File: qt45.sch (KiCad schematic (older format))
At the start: 106 parts, among them SW1 SW_PUSH, U1 ATmega32U4-AU, Y1 16MHz

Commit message: Layout key switches
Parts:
- removed MX42: MX-1U, MX_Alps_Hybrid:MXOnly-1U-NoLED, symbol MX_Alps_Hybrids:MX-1U
- added MX42: MX-1.25U, MX_Alps_Hybrid:MXOnly-1.25U-NoLED, symbol MX_Alps_Hybrids:MX-1.25U
- renumbered D5 to D3, D3 to D4, D4 to D5
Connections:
- net COL12: now also MX42.1 (COL)
- net at D42.2 (A): now also MX42.2 (ROW)
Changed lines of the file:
@@
 $EndComp
 $Comp
-L Device:D_Small D3
+L Device:D_Small D4
 U 1 1 5C9F1A36
 P 6500 3725
-F 0 "D3" H 6500 3875 50  0000 R CNN
+F 0 "D4" H 6500 3875 50  0000 R CNN
 F 1 "SOD-123" H 6900 3875 50  0000 R CNN
 F 2 "random-keyboard-parts:D_SOD-123-Pretty" V 6500 3725 50  0001 C CNN
@@
 $EndComp
 $Comp
-L Device:D_Small D4
+L Device:D_Small D5
 U 1 1 5C9F3E7F
 P 6500 4475
-F 0 "D4" H 6500 4625 50  0000 R CNN
+F 0 "D5" H 6500 4625 50  0000 R CNN
 F 1 "SOD-123" H 6900 4625 50  0000 R CNN
 F 2 "random-keyboard-parts:D_SOD-123-Pretty" V 6500 4475 50  0001 C CNN
@@
 COL13
 $Comp
-L Device:D_Small D5
+L Device:D_Small D3
 U 1 1 5C9E3060
 P 5750 5225
-F 0 "D5" H 5750 5375 50  0000 R CNN
+F 0 "D3" H 5750 5375 50  0000 R CNN
 F 1 "SOD-123" H 6150 5375 50  0000 R CNN
 F 2 "random-keyboard-parts:D_SOD-123-Pretty" V 5750 5225 50  0001 C CNN
@@
 Wire Wire Line
 	14300 4925 14300 4175
-$Comp
-L MX_Alps_Hybrids:MX-1U MX42
-U 1 1 5CA77763
-P 14875 4950
-F 0 "MX42" H 14961 5167 60  0000 C CNN
-F 1 "MX-1U" H 14961 5093 20  0000 C CNN
-F 2 "MX_Alps_Hybrid:MXOnly-1U-NoLED" H 14850 4925 60  0001 C CNN
-F 3 "" H 14850 4925 60  0001 C CNN
-	1    14875 4950
-	1    0    0    -1
-$EndComp
 $Comp
 L Device:D_Small D42
@@
 	14300 5675 14300 4925
 Connection ~ 14300 4925
+$Comp
+L MX_Alps_Hybrids:MX-1.25U MX42
+U 1 1 5CB0FADC
+P 14875 4950
+F 0 "MX42" H 14961 5167 60  0000 C CNN
+F 1 "MX-1.25U" H 14961 5093 20  0000 C CNN
+F 2 "MX_Alps_Hybrid:MXOnly-1.25U-NoLED" H 14850 4925 60  0001 C CNN
+F 3 "" H 14850 4925 60  0001 C CNN
+	1    14875 4950
+	1    0    0    -1
+$EndComp
 $EndSCHEMATC

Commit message: Rough placement of components
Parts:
- MX23: footprint MX_Alps_Hybrid:MXOnly-6.25U-NoLED -> MX_Alps_Hybrid:MXOnly-6.25U-ReversedStabilizers-NoLED
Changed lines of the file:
@@
 F 0 "MX23" H 10461 5917 60  0000 C CNN
 F 1 "MX-6.25U" H 10461 5843 20  0000 C CNN
-F 2 "MX_Alps_Hybrid:MXOnly-6.25U-NoLED" H 10350 5675 60  0001 C CNN
+F 2 "MX_Alps_Hybrid:MXOnly-6.25U-ReversedStabilizers-NoLED" H 10350 5675 60  0001 C CNN
 F 3 "" H 10350 5675 60  0001 C CNN
 	1    10375 5700

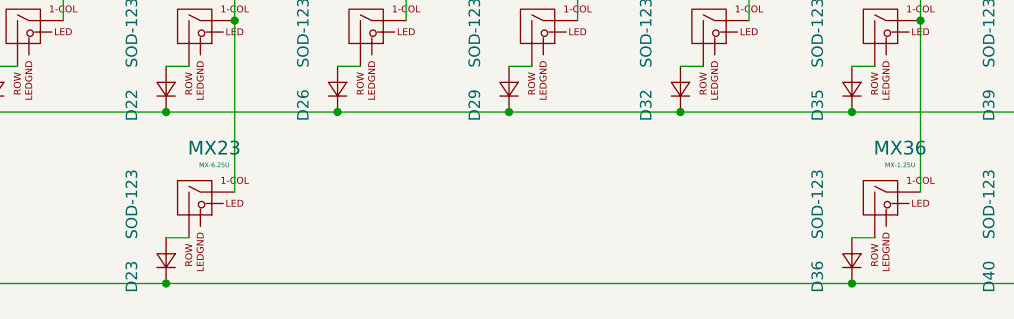
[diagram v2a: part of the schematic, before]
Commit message: Routing (no rows and columns)
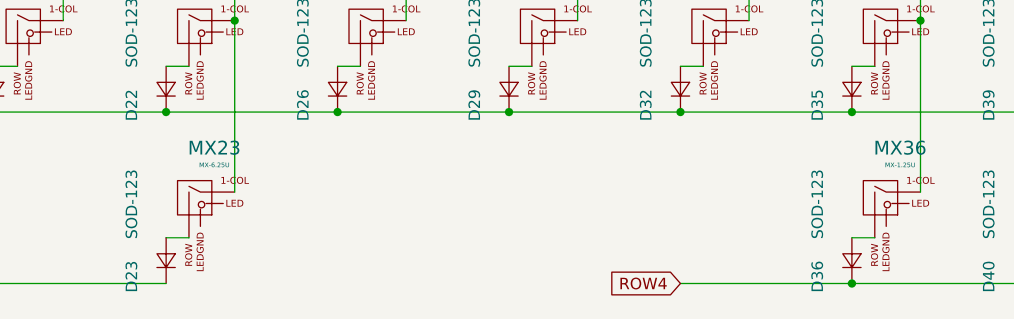
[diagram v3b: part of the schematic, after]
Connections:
- net ROW3: no longer D36.1 (K), D40.1 (K)
- new net ROW4: D36.1 (K), D40.1 (K)
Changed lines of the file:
@@
 	13250 5875 13350 5875
-Wire Wire Line
-	13250 6075 10250 6075
 Wire Wire Line
 	13550 5675 13550 4925
@@
 Wire Wire Line
 	14000 6075 13250 6075
-Connection ~ 10250 6075
-Connection ~ 13250 6075
 $Comp
 L MX_Alps_Hybrids:MX-1.25U MX36
@@
 	1    0    0    -1
 $EndComp
+Text GLabel 12500 6075 0    50   Input ~ 0
+ROW4
+Wire Wire Line
+	13250 6075 12500 6075
+Connection ~ 13250 6075
 $EndSCHEMATC

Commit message: Start reroute
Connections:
- net COL6: no longer MX23.1 (COL)
- net COL7: now also MX23.1 (COL)
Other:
- moved on the sheet: D23, MX23
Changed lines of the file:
@@
 L Device:D_Small D23
 U 1 1 5CA86F72
-P 10250 5975
-F 0 "D23" H 10250 6125 50  0000 R CNN
-F 1 "SOD-123" H 10650 6125 50  0000 R CNN
-F 2 "random-keyboard-parts:D_SOD-123-Pretty" V 10250 5975 50  0001 C CNN
-F 3 "~" V 10250 5975 50  0001 C CNN
-	1    10250 5975
+P 11000 5975
+F 0 "D23" H 11000 6125 50  0000 R CNN
+F 1 "SOD-123" H 11400 6125 50  0000 R CNN
+F 2 "random-keyboard-parts:D_SOD-123-Pretty" V 11000 5975 50  0001 C CNN
+F 3 "~" V 11000 5975 50  0001 C CNN
+	1    11000 5975
 	0    -1   -1   0
 $EndComp
 Wire Wire Line
-	10250 5875 10350 5875
+	11000 5875 11100 5875
 Wire Wire Line
-	10250 6075 8000 6075
+	11000 6075 8000 6075
 Wire Wire Line
-	10550 5675 10550 4925
+	11300 5675 11300 4925
 $Comp
 L MX_Alps_Hybrids:MX-6.25U MX23
 U 1 1 5CA8EADA
-P 10375 5700
-F 0 "MX23" H 10461 5917 60  0000 C CNN
-F 1 "MX-6.25U" H 10461 5843 20  0000 C CNN
-F 2 "MX_Alps_Hybrid:MXOnly-6.25U-ReversedStabilizers-NoLED" H 10350 5675 60  0001 C CNN
-F 3 "" H 10350 5675 60  0001 C CNN
-	1    10375 5700
+P 11125 5700
+F 0 "MX23" H 11211 5917 60  0000 C CNN
+F 1 "MX-6.25U" H 11211 5843 20  0000 C CNN
+F 2 "MX_Alps_Hybrid:MXOnly-6.25U-ReversedStabilizers-NoLED" H 11100 5675 60  0001 C CNN
+F 3 "" H 11100 5675 60  0001 C CNN
+	1    11125 5700
 	1    0    0    -1
 $EndComp
-Connection ~ 8000 6075
 $Comp
 L Device:D_Small D36
@@
 Connection ~ 9500 5325
 Connection ~ 10250 5325
-Connection ~ 10550 4925
 Connection ~ 11000 5325
 Connection ~ 11750 5325
@@
 	13250 6075 12500 6075
 Connection ~ 13250 6075
+Connection ~ 11300 4925
+Connection ~ 8000 6075
 $EndSCHEMATC

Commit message: More routing
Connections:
- net COL0: now also U1.31 (PC6)
- net COL1: now also U1.32 (PC7)
- net COL2: now also U1.30 (PB6)
- net COL3: now also U1.29 (PB5)
- net COL4: now also U1.28 (PB4)
- net COL5: now also U1.22 (PD5)
- net COL6: now also U1.27 (PD7)
- net ROW0: now also U1.19 (PD1)
- net ROW1: now also U1.20 (PD2)
- net ROW2: now also U1.21 (PD3)
- net ROW3: now also U1.18 (PD0); no longer D23.1 (K)
- net ROW4: now also D23.1 (K)
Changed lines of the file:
@@
 	11000 5875 11100 5875
-Wire Wire Line
-	11000 6075 8000 6075
 Wire Wire Line
 	11300 5675 11300 4925
@@
 	1    0    0    -1
 $EndComp
-Text GLabel 12500 6075 0    50   Input ~ 0
+Text GLabel 10250 6075 0    50   Input ~ 0
 ROW4
 Wire Wire Line
-	13250 6075 12500 6075
+	13250 6075 11000 6075
 Connection ~ 13250 6075
 Connection ~ 11300 4925
-Connection ~ 8000 6075
+Connection ~ 11000 6075
+Wire Wire Line
+	11000 6075 10250 6075
+Text GLabel 3350 3850 2    50   Input ~ 0
+COL6
+Text GLabel 3350 3650 2    50   Input ~ 0
+COL5
+Text GLabel 3350 2350 2    50   Input ~ 0
+COL4
+Text GLabel 3350 2450 2    50   Input ~ 0
+COL3
+Text GLabel 3350 2550 2    50   Input ~ 0
+COL2
+Text GLabel 3350 2950 2    50   Input ~ 0
+COL1
+Text GLabel 3350 2850 2    50   Input ~ 0
+COL0
+Text GLabel 3350 3450 2    50   Input ~ 0
+ROW2
+Text GLabel 3350 3350 2    50   Input ~ 0
+ROW1
+Text GLabel 3350 3150 2    50   Input ~ 0
+ROW3
+Text GLabel 3350 3250 2    50   Input ~ 0
+ROW0
 $EndSCHEMATC

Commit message: First draft of routing
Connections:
- net ROW4 is gone; now on net ROW3: D23.1 (K), D36.1 (K), D40.1 (K)
- net COL0: now also U1.29 (PB5); no longer U1.31 (PC6)
- net COL1: now also U1.30 (PB6); no longer U1.32 (PC7)
- net COL10: now also U1.38 (PF5)
- net COL11: now also U1.1 (PE6)
- net COL12: now also U1.39 (PF4)
- net COL13: now also U1.40 (PF1)
- net COL2: now also U1.28 (PB4); no longer U1.30 (PB6)
- net COL3: now also U1.27 (PD7); no longer U1.29 (PB5)
- net COL4: now also U1.26 (PD6); no longer U1.28 (PB4)
- net COL6: now also U1.25 (PD4); no longer U1.27 (PD7)
- net COL7: now also U1.41 (PF0)
- net COL8: now also U1.36 (PF7)
- net COL9: now also U1.37 (PF6)
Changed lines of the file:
@@
 	1    0    0    -1
 $EndComp
-Text GLabel 10250 6075 0    50   Input ~ 0
-ROW4
 Wire Wire Line
 	13250 6075 11000 6075
@@
 Connection ~ 11000 6075
 Wire Wire Line
-	11000 6075 10250 6075
-Text GLabel 3350 3850 2    50   Input ~ 0
+	11000 6075 8000 6075
+Text GLabel 3350 3550 2    50   Input ~ 0
 COL6
 Text GLabel 3350 3650 2    50   Input ~ 0
 COL5
-Text GLabel 3350 2350 2    50   Input ~ 0
+Text GLabel 3350 3750 2    50   Input ~ 0
 COL4
-Text GLabel 3350 2450 2    50   Input ~ 0
+Text GLabel 3350 3850 2    50   Input ~ 0
 COL3
 Text GLabel 3350 2550 2    50   Input ~ 0
-COL2
-Text GLabel 3350 2950 2    50   Input ~ 0
 COL1
-Text GLabel 3350 2850 2    50   Input ~ 0
+Text GLabel 3350 2450 2    50   Input ~ 0
 COL0
 Text GLabel 3350 3450 2    50   Input ~ 0
@@
 Text GLabel 3350 3250 2    50   Input ~ 0
 ROW0
+Connection ~ 8000 6075
+Text GLabel 3350 4150 2    50   Input ~ 0
+COL11
+Text GLabel 3350 2350 2    50   Input ~ 0
+COL2
+Text GLabel 3350 4350 2    50   Input ~ 0
+COL7
+Text GLabel 3350 4450 2    50   Input ~ 0
+COL13
+Text GLabel 3350 4550 2    50   Input ~ 0
+COL12
+Text GLabel 3350 4650 2    50   Input ~ 0
+COL10
+Text GLabel 3350 4750 2    50   Input ~ 0
+COL9
+Text GLabel 3350 4850 2    50   Input ~ 0
+COL8
 $EndSCHEMATC

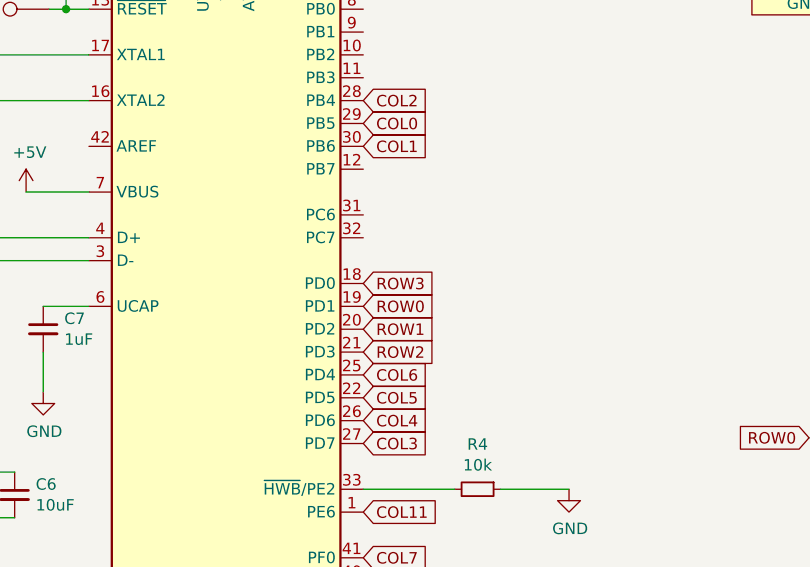
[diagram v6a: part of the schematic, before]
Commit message: Re-route to maximise ground plane
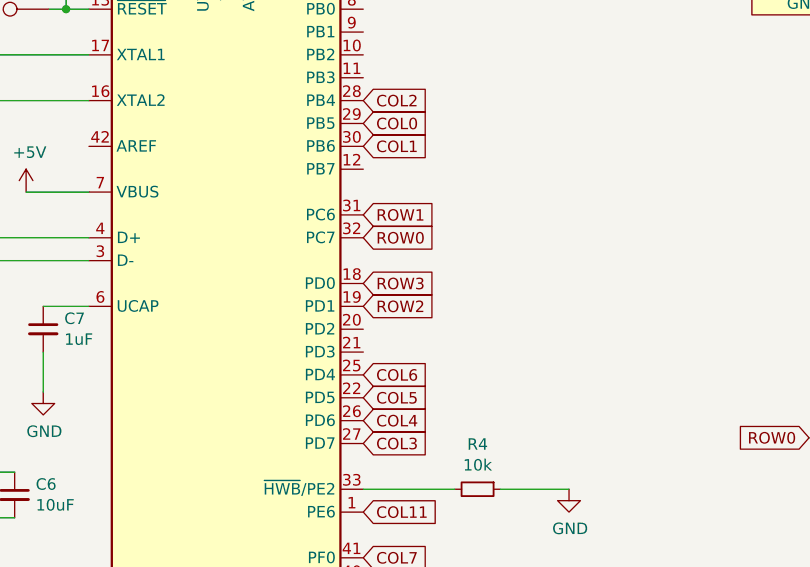
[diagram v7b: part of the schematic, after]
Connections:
- net ROW0: now also U1.32 (PC7); no longer U1.19 (PD1)
- net ROW1: now also U1.31 (PC6); no longer U1.20 (PD2)
- net ROW2: now also U1.19 (PD1); no longer U1.21 (PD3)
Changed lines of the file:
@@
 EESchema Schematic File Version 4
+LIBS:qt45-cache
 EELAYER 29 0
 EELAYER END
@@
 Text GLabel 3350 2450 2    50   Input ~ 0
 COL0
-Text GLabel 3350 3450 2    50   Input ~ 0
+Text GLabel 3350 3250 2    50   Input ~ 0
 ROW2
-Text GLabel 3350 3350 2    50   Input ~ 0
+Text GLabel 3350 2850 2    50   Input ~ 0
 ROW1
 Text GLabel 3350 3150 2    50   Input ~ 0
 ROW3
-Text GLabel 3350 3250 2    50   Input ~ 0
+Text GLabel 3350 2950 2    50   Input ~ 0
 ROW0
 Connection ~ 8000 6075

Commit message: Fix some issues
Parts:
- MX1, MX10, MX11, MX12, MX14, MX15, MX16, MX17, MX18, MX19, MX20, MX21, MX22, MX24, MX25, MX26, MX27, MX28, MX29, MX30, MX31, MX32, MX33, MX34, MX35, MX37, MX38, MX39, MX4, MX40, MX41, MX43, MX45, MX5, MX6, MX7, MX8, MX9: symbol MX_Alps_Hybrids:MX-1U -> qt45-rescue:MX-1U-MX_Alps_Hybrids
- MX13, MX2, MX36, MX42: symbol MX_Alps_Hybrids:MX-1.25U -> qt45-rescue:MX-1.25U-MX_Alps_Hybrids
- MX23: symbol MX_Alps_Hybrids:MX-6.25U -> qt45-rescue:MX-6.25U-MX_Alps_Hybrids
- MX3, MX44: symbol MX_Alps_Hybrids:MX-1.75U -> qt45-rescue:MX-1.75U-MX_Alps_Hybrids
- USB1: symbol random-keyboard-parts:Molex-0548190589 -> qt45-rescue:Molex-0548190589-random-keyboard-parts
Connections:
- net ROW2: now also U1.21 (PD3); no longer U1.19 (PD1)
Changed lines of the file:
@@
 D-
 $Comp
-L random-keyboard-parts:Molex-0548190589 USB1
+L qt45-rescue:Molex-0548190589-random-keyboard-parts USB1
 U 1 1 5C9D7E35
 P 5300 1725
@@
 	6300 1525 6600 1525
 $Comp
-L MX_Alps_Hybrids:MX-1U MX1
+L qt45-rescue:MX-1U-MX_Alps_Hybrids MX1
 U 1 1 5C9E3362
 P 5875 3450
@@
 	5750 3625 5850 3625
 $Comp
-L MX_Alps_Hybrids:MX-1U MX4
+L qt45-rescue:MX-1U-MX_Alps_Hybrids MX4
 U 1 1 5C9F1A30
 P 6625 3450
@@
 	5750 4375 5850 4375
 $Comp
-L MX_Alps_Hybrids:MX-1U MX5
+L qt45-rescue:MX-1U-MX_Alps_Hybrids MX5
 U 1 1 5C9F3E79
 P 6625 4200
@@
 	5600 1925 5750 1925
 $Comp
-L MX_Alps_Hybrids:MX-1.25U MX2
+L qt45-rescue:MX-1.25U-MX_Alps_Hybrids MX2
 U 1 1 5C9B916B
 P 5875 4200
@@
 $EndComp
 $Comp
-L MX_Alps_Hybrids:MX-1U MX6
+L qt45-rescue:MX-1U-MX_Alps_Hybrids MX6
 U 1 1 5C9BC6F1
 P 7375 3450
@@
 	7550 3425 7550 2925
 $Comp
-L MX_Alps_Hybrids:MX-1U MX10
+L qt45-rescue:MX-1U-MX_Alps_Hybrids MX10
 U 1 1 5C9BE4D7
 P 8125 3450
@@
 	8300 3425 8300 2925
 $Comp
-L MX_Alps_Hybrids:MX-1U MX14
+L qt45-rescue:MX-1U-MX_Alps_Hybrids MX14
 U 1 1 5C9C001E
 P 8875 3450
@@
 	9050 3425 9050 2925
 $Comp
-L MX_Alps_Hybrids:MX-1U MX17
+L qt45-rescue:MX-1U-MX_Alps_Hybrids MX17
 U 1 1 5C9C1BBC
 P 9625 3450
@@
 	9800 3425 9800 2925
 $Comp
-L MX_Alps_Hybrids:MX-1U MX20
+L qt45-rescue:MX-1U-MX_Alps_Hybrids MX20
 U 1 1 5C9C3BA7
 P 10375 3450
@@
 	10550 3425 10550 2925
 $Comp
-L MX_Alps_Hybrids:MX-1U MX24
+L qt45-rescue:MX-1U-MX_Alps_Hybrids MX24
 U 1 1 5C9C5CC1
 P 11125 3450
@@
 	11300 3425 11300 2925
 $Comp
-L MX_Alps_Hybrids:MX-1U MX27
+L qt45-rescue:MX-1U-MX_Alps_Hybrids MX27
 U 1 1 5C9C7E50
 P 11875 3450
@@
 	12050 3425 12050 2925
 $Comp
-L MX_Alps_Hybrids:MX-1U MX30
+L qt45-rescue:MX-1U-MX_Alps_Hybrids MX30
 U 1 1 5C9CA35D
 P 12625 3450
@@
 	12800 3425 12800 2925
 $Comp
-L MX_Alps_Hybrids:MX-1U MX33
+L qt45-rescue:MX-1U-MX_Alps_Hybrids MX33
 U 1 1 5C9CC78F
 P 13375 3450
@@
 	13250 3825 12500 3825
 $Comp
-L MX_Alps_Hybrids:MX-1U MX37
+L qt45-rescue:MX-1U-MX_Alps_Hybrids MX37
 U 1 1 5C9D15CD
 P 14125 3450
@@
 	14300 3425 14300 2925
 $Comp
-L MX_Alps_Hybrids:MX-1U MX41
+L qt45-rescue:MX-1U-MX_Alps_Hybrids MX41
 U 1 1 5C9D401D
 P 14875 3450
@@
 	15050 3425 15050 2925
 $Comp
-L MX_Alps_Hybrids:MX-1U MX43
+L qt45-rescue:MX-1U-MX_Alps_Hybrids MX43
 U 1 1 5C9D6C8C
 P 15625 3450
@@
 	6050 4925 6050 4175
 $Comp
-L MX_Alps_Hybrids:MX-1.75U MX3
+L qt45-rescue:MX-1.75U-MX_Alps_Hybrids MX3
 U 1 1 5C9E57C6
 P 5875 4950
@@
 	15800 4175 15800 3425
 $Comp
-L MX_Alps_Hybrids:MX-1U MX45
+L qt45-rescue:MX-1U-MX_Alps_Hybrids MX45
 U 1 1 5C9EDC9E
 P 15625 4950
@@
 	15800 4925 15800 4175
 $Comp
-L MX_Alps_Hybrids:MX-1.75U MX44
+L qt45-rescue:MX-1.75U-MX_Alps_Hybrids MX44
 U 1 1 5C9F5826
 P 15625 4200
@@
 Connection ~ 15800 4175
 $Comp
-L MX_Alps_Hybrids:MX-1U MX7
+L qt45-rescue:MX-1U-MX_Alps_Hybrids MX7
 U 1 1 5C9F740B
 P 7375 4200
@@
 	7550 4175 7550 3425
 $Comp
-L MX_Alps_Hybrids:MX-1U MX11
+L qt45-rescue:MX-1U-MX_Alps_Hybrids MX11
 U 1 1 5C9FAD4C
 P 8125 4200
@@
 	8300 4175 8300 3425
 $Comp
-L MX_Alps_Hybrids:MX-1U MX15
+L qt45-rescue:MX-1U-MX_Alps_Hybrids MX15
 U 1 1 5C9FE4FA
 P 8875 4200
@@
 	9050 4175 9050 3425
 $Comp
-L MX_Alps_Hybrids:MX-1U MX18
+L qt45-rescue:MX-1U-MX_Alps_Hybrids MX18
 U 1 1 5CA01E5D
 P 9625 4200
@@
 	9800 4175 9800 3425
 $Comp
-L MX_Alps_Hybrids:MX-1U MX21
+L qt45-rescue:MX-1U-MX_Alps_Hybrids MX21
 U 1 1 5CA0574C
 P 10375 4200
@@
 	10550 4175 10550 3425
 $Comp
-L MX_Alps_Hybrids:MX-1U MX25
+L qt45-rescue:MX-1U-MX_Alps_Hybrids MX25
 U 1 1 5CA095A9
 P 11125 4200
@@
 	11300 4175 11300 3425
 $Comp
-L MX_Alps_Hybrids:MX-1U MX28
+L qt45-rescue:MX-1U-MX_Alps_Hybrids MX28
 U 1 1 5CA0D728
 P 11875 4200
@@
 	12050 4175 12050 3425
 $Comp
-L MX_Alps_Hybrids:MX-1U MX31
+L qt45-rescue:MX-1U-MX_Alps_Hybrids MX31
 U 1 1 5CA11F75
 P 12625 4200
@@
 	12800 4175 12800 3425
 $Comp
-L MX_Alps_Hybrids:MX-1U MX34
+L qt45-rescue:MX-1U-MX_Alps_Hybrids MX34
 U 1 1 5CA166A4
 P 13375 4200
@@
 	13550 4175 13550 3425
 $Comp
-L MX_Alps_Hybrids:MX-1U MX38
+L qt45-rescue:MX-1U-MX_Alps_Hybrids MX38
 U 1 1 5CA1B18A
 P 14125 4200
@@
 Connection ~ 14000 4575
 $Comp
-L MX_Alps_Hybrids:MX-1U MX8
+L qt45-rescue:MX-1U-MX_Alps_Hybrids MX8
 U 1 1 5CA251B8
 P 7375 4950
@@
 	5750 5325 7250 5325
 $Comp
-L MX_Alps_Hybrids:MX-1U MX9
+L qt45-rescue:MX-1U-MX_Alps_Hybrids MX9
 U 1 1 5CA2A17F
 P 7375 5700
@@
 ROW3
 $Comp
-L MX_Alps_Hybrids:MX-1U MX12
+L qt45-rescue:MX-1U-MX_Alps_Hybrids MX12
 U 1 1 5CA35694
 P 8125 4950
@@
 	8300 5675 8300 4925
 $Comp
-L MX_Alps_Hybrids:MX-1.25U MX13
+L qt45-rescue:MX-1.25U-MX_Alps_Hybrids MX13
 U 1 1 5CA4021B
 P 8125 5700
@@
 $EndComp
 $Comp
-L MX_Alps_Hybrids:MX-1U MX16
+L qt45-rescue:MX-1U-MX_Alps_Hybrids MX16
 U 1 1 5CA4189F
 P 8875 4950
@@
 	9050 4925 9050 4175
 $Comp
-L MX_Alps_Hybrids:MX-1U MX19
+L qt45-rescue:MX-1U-MX_Alps_Hybrids MX19
 U 1 1 5CA4792D
 P 9625 4950
@@
 	9800 4925 9800 4175
 $Comp
-L MX_Alps_Hybrids:MX-1U MX22
+L qt45-rescue:MX-1U-MX_Alps_Hybrids MX22
 U 1 1 5CA4DB14
 P 10375 4950
@@
 	10550 4925 10550 4175
 $Comp
-L MX_Alps_Hybrids:MX-1U MX26
+L qt45-rescue:MX-1U-MX_Alps_Hybrids MX26
 U 1 1 5CA5404F
 P 11125 4950
@@
 	11300 4925 11300 4175
 $Comp
-L MX_Alps_Hybrids:MX-1U MX29
+L qt45-rescue:MX-1U-MX_Alps_Hybrids MX29
 U 1 1 5CA5AB30
 P 11875 4950
@@
 	12050 4925 12050 4175
 $Comp
-L MX_Alps_Hybrids:MX-1U MX32
+L qt45-rescue:MX-1U-MX_Alps_Hybrids MX32
 U 1 1 5CA61676
 P 12625 4950
@@
 	12800 4925 12800 4175
 $Comp
-L MX_Alps_Hybrids:MX-1U MX35
+L qt45-rescue:MX-1U-MX_Alps_Hybrids MX35
 U 1 1 5CA688E9
 P 13375 4950
@@
 	13550 4925 13550 4175
 $Comp
-L MX_Alps_Hybrids:MX-1U MX39
+L qt45-rescue:MX-1U-MX_Alps_Hybrids MX39
 U 1 1 5CA6FE30
 P 14125 4950
@@
 	11300 5675 11300 4925
 $Comp
-L MX_Alps_Hybrids:MX-6.25U MX23
+L qt45-rescue:MX-6.25U-MX_Alps_Hybrids MX23
 U 1 1 5CA8EADA
 P 11125 5700
@@
 	13550 5675 13550 4925
 $Comp
-L MX_Alps_Hybrids:MX-1U MX40
+L qt45-rescue:MX-1U-MX_Alps_Hybrids MX40
 U 1 1 5CAA04DD
 P 14125 5700
@@
 	14000 6075 13250 6075
 $Comp
-L MX_Alps_Hybrids:MX-1.25U MX36
+L qt45-rescue:MX-1.25U-MX_Alps_Hybrids MX36
 U 1 1 5CAB0986
 P 13375 5700
@@
 Connection ~ 14300 4925
 $Comp
-L MX_Alps_Hybrids:MX-1.25U MX42
+L qt45-rescue:MX-1.25U-MX_Alps_Hybrids MX42
 U 1 1 5CB0FADC
 P 14875 4950
@@
 Text GLabel 3350 2450 2    50   Input ~ 0
 COL0
-Text GLabel 3350 3250 2    50   Input ~ 0
+Text GLabel 3350 3450 2    50   Input ~ 0
 ROW2
 Text GLabel 3350 2850 2    50   Input ~ 0
